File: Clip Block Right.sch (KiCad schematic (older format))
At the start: 18 parts, among them J16 Conn_01x08_Female, SW17 SW_SPST_4_PIN, SW18 SW_SPST_4_PIN, SW19 SW_SPST_4_PIN, SW20 SW_SPST_4_PIN, SW21 SW_SPST_4_PIN, SW22 SW_SPST_4_PIN, SW23 SW_SPST_4_PIN, SW24 SW_SPST_4_PIN, SW25 SW_SPST_4_PIN, SW26 SW_SPST_4_PIN, SW27 SW_SPST_4_PIN, SW28 SW_SPST_4_PIN, SW29 SW_SPST_4_PIN, SW30 SW_SPST_4_PIN, SW31 SW_SPST_4_PIN, SW32 SW_SPST_4_PIN, U2 CD74HC4067M

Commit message: Further work on the separate boards
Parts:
- SW17, SW18, SW19, SW20, SW21, SW22, SW23, SW24, SW25, SW26, SW27, SW28, SW29, SW30, SW31, SW32: symbol sw_spst_0:SW_SPST_4_PIN -> cp_midi_control_surface_002-rescue:SW_SPST_4_PIN-sw_spst_0
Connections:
- wire segments 114 -> 116
- no-connect marks 33 -> 32
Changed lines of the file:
@@
 $EndDescr
 $Comp
-L sw_spst_0:SW_SPST_4_PIN SW?
-U 1 1 5C60BB5B
-P 5550 1550
-AR Path="/5C4B73B3/5C60BB5B" Ref="SW?"  Part="1"
-AR Path="/5C4B9DB9/5C60BB5B" Ref="SW17"  Part="1"
-F 0 "SW17" H 5550 1300 50  0000 C CNN
-F 1 "SW_SPST_4_PIN" H 5550 1724 50  0001 C CNN
-F 2 "cunabulapress-footprints:Omron_B3F-5050" H 5550 1700 50  0001 C CNN
-F 3 "" H 5550 1700 50  0001 C CNN
-	1    5550 1550
-	1    0    0    -1
-$EndComp
-$Comp
-L sw_spst_0:SW_SPST_4_PIN SW?
+L cp_midi_control_surface_002-rescue:SW_SPST_4_PIN-sw_spst_0 SW?
 U 1 1 5C60BB62
 P 5550 2050
 AR Path="/5C4B73B3/5C60BB62" Ref="SW?"  Part="1"
 AR Path="/5C4B9DB9/5C60BB62" Ref="SW18"  Part="1"
+AR Path="/5C60BB62" Ref="SW18"  Part="1"
 F 0 "SW18" H 5550 1850 50  0000 C CNN
 F 1 "SW_SPST_4_PIN" H 5550 2224 50  0001 C CNN
@@
 $EndComp
 $Comp
-L sw_spst_0:SW_SPST_4_PIN SW?
+L cp_midi_control_surface_002-rescue:SW_SPST_4_PIN-sw_spst_0 SW?
 U 1 1 5C60BB69
 P 5550 2550
 AR Path="/5C4B73B3/5C60BB69" Ref="SW?"  Part="1"
 AR Path="/5C4B9DB9/5C60BB69" Ref="SW19"  Part="1"
+AR Path="/5C60BB69" Ref="SW19"  Part="1"
 F 0 "SW19" H 5550 2350 50  0000 C CNN
 F 1 "SW_SPST_4_PIN" H 5550 2724 50  0001 C CNN
@@
 $EndComp
 $Comp
-L sw_spst_0:SW_SPST_4_PIN SW?
+L cp_midi_control_surface_002-rescue:SW_SPST_4_PIN-sw_spst_0 SW?
 U 1 1 5C60BB70
 P 5550 3050
 AR Path="/5C4B73B3/5C60BB70" Ref="SW?"  Part="1"
 AR Path="/5C4B9DB9/5C60BB70" Ref="SW20"  Part="1"
+AR Path="/5C60BB70" Ref="SW20"  Part="1"
 F 0 "SW20" H 5550 2850 50  0000 C CNN
 F 1 "SW_SPST_4_PIN" H 5550 3224 50  0001 C CNN
@@
 $EndComp
 $Comp
-L sw_spst_0:SW_SPST_4_PIN SW?
+L cp_midi_control_surface_002-rescue:SW_SPST_4_PIN-sw_spst_0 SW?
 U 1 1 5C60BB77
 P 5550 3550
 AR Path="/5C4B73B3/5C60BB77" Ref="SW?"  Part="1"
 AR Path="/5C4B9DB9/5C60BB77" Ref="SW21"  Part="1"
+AR Path="/5C60BB77" Ref="SW21"  Part="1"
 F 0 "SW21" H 5550 3350 50  0000 C CNN
 F 1 "SW_SPST_4_PIN" H 5550 3724 50  0001 C CNN
@@
 $EndComp
 $Comp
-L sw_spst_0:SW_SPST_4_PIN SW?
+L cp_midi_control_surface_002-rescue:SW_SPST_4_PIN-sw_spst_0 SW?
 U 1 1 5C60BB7E
 P 5550 4050
 AR Path="/5C4B73B3/5C60BB7E" Ref="SW?"  Part="1"
 AR Path="/5C4B9DB9/5C60BB7E" Ref="SW22"  Part="1"
+AR Path="/5C60BB7E" Ref="SW22"  Part="1"
 F 0 "SW22" H 5550 3850 50  0000 C CNN
 F 1 "SW_SPST_4_PIN" H 5550 4224 50  0001 C CNN
@@
 $EndComp
 $Comp
-L sw_spst_0:SW_SPST_4_PIN SW?
+L cp_midi_control_surface_002-rescue:SW_SPST_4_PIN-sw_spst_0 SW?
 U 1 1 5C60BB85
 P 5550 4550
 AR Path="/5C4B73B3/5C60BB85" Ref="SW?"  Part="1"
 AR Path="/5C4B9DB9/5C60BB85" Ref="SW23"  Part="1"
+AR Path="/5C60BB85" Ref="SW23"  Part="1"
 F 0 "SW23" H 5550 4350 50  0000 C CNN
 F 1 "SW_SPST_4_PIN" H 5550 4724 50  0001 C CNN
@@
 $EndComp
 $Comp
-L sw_spst_0:SW_SPST_4_PIN SW?
+L cp_midi_control_surface_002-rescue:SW_SPST_4_PIN-sw_spst_0 SW?
 U 1 1 5C60BB8C
 P 5550 5050
 AR Path="/5C4B73B3/5C60BB8C" Ref="SW?"  Part="1"
 AR Path="/5C4B9DB9/5C60BB8C" Ref="SW24"  Part="1"
+AR Path="/5C60BB8C" Ref="SW24"  Part="1"
 F 0 "SW24" H 5550 4850 50  0000 C CNN
 F 1 "SW_SPST_4_PIN" H 5550 5224 50  0001 C CNN
@@
 $EndComp
 $Comp
-L sw_spst_0:SW_SPST_4_PIN SW?
+L cp_midi_control_surface_002-rescue:SW_SPST_4_PIN-sw_spst_0 SW?
 U 1 1 5C60BB93
 P 4050 2350
 AR Path="/5C4B73B3/5C60BB93" Ref="SW?"  Part="1"
 AR Path="/5C4B9DB9/5C60BB93" Ref="SW25"  Part="1"
+AR Path="/5C60BB93" Ref="SW25"  Part="1"
 F 0 "SW25" H 4050 2150 50  0000 C CNN
 F 1 "SW_SPST_4_PIN" H 4750 2300 50  0001 C CNN
@@
 $EndComp
 $Comp
-L sw_spst_0:SW_SPST_4_PIN SW?
+L cp_midi_control_surface_002-rescue:SW_SPST_4_PIN-sw_spst_0 SW?
 U 1 1 5C60BB9A
 P 4050 2850
 AR Path="/5C4B73B3/5C60BB9A" Ref="SW?"  Part="1"
 AR Path="/5C4B9DB9/5C60BB9A" Ref="SW26"  Part="1"
+AR Path="/5C60BB9A" Ref="SW26"  Part="1"
 F 0 "SW26" H 4050 2650 50  0000 C CNN
 F 1 "SW_SPST_4_PIN" H 4050 3024 50  0001 C CNN
@@
 $EndComp
 $Comp
-L sw_spst_0:SW_SPST_4_PIN SW?
+L cp_midi_control_surface_002-rescue:SW_SPST_4_PIN-sw_spst_0 SW?
 U 1 1 5C60BBA8
 P 4050 3850
 AR Path="/5C4B73B3/5C60BBA8" Ref="SW?"  Part="1"
 AR Path="/5C4B9DB9/5C60BBA8" Ref="SW28"  Part="1"
+AR Path="/5C60BBA8" Ref="SW28"  Part="1"
 F 0 "SW28" H 4050 3650 50  0000 C CNN
 F 1 "SW_SPST_4_PIN" H 4050 4024 50  0001 C CNN
@@
 $EndComp
 $Comp
-L sw_spst_0:SW_SPST_4_PIN SW?
+L cp_midi_control_surface_002-rescue:SW_SPST_4_PIN-sw_spst_0 SW?
 U 1 1 5C60BBAF
 P 4050 4350
 AR Path="/5C4B73B3/5C60BBAF" Ref="SW?"  Part="1"
 AR Path="/5C4B9DB9/5C60BBAF" Ref="SW29"  Part="1"
+AR Path="/5C60BBAF" Ref="SW29"  Part="1"
 F 0 "SW29" H 4050 4150 50  0000 C CNN
 F 1 "SW_SPST_4_PIN" H 4050 4524 50  0001 C CNN
@@
 $EndComp
 $Comp
-L sw_spst_0:SW_SPST_4_PIN SW?
+L cp_midi_control_surface_002-rescue:SW_SPST_4_PIN-sw_spst_0 SW?
 U 1 1 5C60BBB6
 P 4050 4850
 AR Path="/5C4B73B3/5C60BBB6" Ref="SW?"  Part="1"
 AR Path="/5C4B9DB9/5C60BBB6" Ref="SW30"  Part="1"
+AR Path="/5C60BBB6" Ref="SW30"  Part="1"
 F 0 "SW30" H 4050 4650 50  0000 C CNN
 F 1 "SW_SPST_4_PIN" H 4050 5024 50  0001 C CNN
@@
 $EndComp
 $Comp
-L sw_spst_0:SW_SPST_4_PIN SW?
+L cp_midi_control_surface_002-rescue:SW_SPST_4_PIN-sw_spst_0 SW?
 U 1 1 5C60BBBD
 P 4050 5350
 AR Path="/5C4B73B3/5C60BBBD" Ref="SW?"  Part="1"
 AR Path="/5C4B9DB9/5C60BBBD" Ref="SW31"  Part="1"
+AR Path="/5C60BBBD" Ref="SW31"  Part="1"
 F 0 "SW31" H 4050 5150 50  0000 C CNN
 F 1 "SW_SPST_4_PIN" H 4050 5524 50  0001 C CNN
@@
 $EndComp
 $Comp
-L sw_spst_0:SW_SPST_4_PIN SW?
+L cp_midi_control_surface_002-rescue:SW_SPST_4_PIN-sw_spst_0 SW?
 U 1 1 5C60BBC4
 P 4050 5850
 AR Path="/5C4B73B3/5C60BBC4" Ref="SW?"  Part="1"
 AR Path="/5C4B9DB9/5C60BBC4" Ref="SW32"  Part="1"
+AR Path="/5C60BBC4" Ref="SW32"  Part="1"
 F 0 "SW32" H 4050 5650 50  0000 C CNN
 F 1 "SW_SPST_4_PIN" H 4050 6024 50  0001 C CNN
@@
 	2650 2750 3400 2750
 Wire Wire Line
-	3400 2750 3400 4350
-Wire Wire Line
-	3400 4350 3850 4350
-Wire Wire Line
 	2650 2850 3300 2850
-Wire Wire Line
-	3300 2850 3300 4850
-Wire Wire Line
-	3300 4850 3850 4850
 Wire Wire Line
 	2650 2950 3200 2950
@@
 	3500 1800 4800 1800
 Wire Wire Line
-	5000 1700 5000 3050
-Wire Wire Line
-	5100 1650 5100 2550
-Wire Wire Line
-	5200 1600 5200 2050
-Wire Wire Line
-	5200 2050 5350 2050
-Wire Wire Line
-	2650 1550 5350 1550
-Wire Wire Line
-	5100 2550 5350 2550
-Wire Wire Line
-	5000 3050 5350 3050
+	2650 1550 5300 1550
 Wire Wire Line
 	3100 1600 5200 1600
@@
 Wire Wire Line
 	2150 3450 2150 3350
-NoConn ~ 5350 1650
-NoConn ~ 5350 2150
-NoConn ~ 5350 2650
-NoConn ~ 5350 3150
 NoConn ~ 5750 4150
 NoConn ~ 5750 3650
@@
 NoConn ~ 4250 3950
 NoConn ~ 4250 4450
-NoConn ~ 3850 4450
-NoConn ~ 3850 4950
 NoConn ~ 4250 4950
 NoConn ~ 4250 5450
@@
 	2650 2350 3800 2350
 $Comp
-L sw_spst_0:SW_SPST_4_PIN SW?
+L cp_midi_control_surface_002-rescue:SW_SPST_4_PIN-sw_spst_0 SW?
 U 1 1 5C60BBA1
 P 4050 3350
 AR Path="/5C4B73B3/5C60BBA1" Ref="SW?"  Part="1"
 AR Path="/5C4B9DB9/5C60BBA1" Ref="SW27"  Part="1"
+AR Path="/5C60BBA1" Ref="SW27"  Part="1"
 F 0 "SW27" H 4050 3150 50  0000 C CNN
 F 1 "SW_SPST_4_PIN" H 4050 3524 50  0001 C CNN
@@
 	3500 2650 3500 3950
 Wire Wire Line
-	4900 3650 5350 3650
-Wire Wire Line
-	4900 1750 4900 3650
-Wire Wire Line
-	4800 4150 5350 4150
-Wire Wire Line
-	4800 1800 4800 4150
+	4900 1750 4900 3550
+Wire Wire Line
+	4800 1800 4800 4050
 Wire Wire Line
 	4700 1850 4700 4550
-Wire Wire Line
-	4600 5150 5350 5150
-Wire Wire Line
-	4600 1900 4600 5150
-NoConn ~ 5350 3550
-NoConn ~ 5350 4050
-NoConn ~ 5350 5050
 Wire Wire Line
 	4700 4550 5350 4550
@@
 	5900 5150 5900 5850
 NoConn ~ 5750 5050
+Wire Wire Line
+	5350 2150 5200 2150
+Wire Wire Line
+	5200 1600 5200 2150
+Wire Wire Line
+	3400 2750 3400 4350
+Wire Wire Line
+	5350 5050 4600 5050
+Wire Wire Line
+	4600 1900 4600 5050
+Wire Wire Line
+	5300 1550 5300 1650
+Wire Wire Line
+	5300 1650 5350 1650
+$Comp
+L cp_midi_control_surface_002-rescue:SW_SPST_4_PIN-sw_spst_0 SW?
+U 1 1 5C60BB5B
+P 5550 1550
+AR Path="/5C4B73B3/5C60BB5B" Ref="SW?"  Part="1"
+AR Path="/5C4B9DB9/5C60BB5B" Ref="SW17"  Part="1"
+AR Path="/5C60BB5B" Ref="SW17"  Part="1"
+F 0 "SW17" H 5550 1300 50  0000 C CNN
+F 1 "SW_SPST_4_PIN" H 5550 1724 50  0001 C CNN
+F 2 "cunabulapress-footprints:Omron_B3F-5050" H 5550 1700 50  0001 C CNN
+F 3 "" H 5550 1700 50  0001 C CNN
+	1    5550 1550
+	1    0    0    -1
+$EndComp
+NoConn ~ 5350 2050
+NoConn ~ 5350 1550
+Wire Wire Line
+	5350 2650 5100 2650
+Wire Wire Line
+	5100 1650 5100 2650
+Wire Wire Line
+	5350 3150 5000 3150
+Wire Wire Line
+	5000 1700 5000 3150
+Wire Wire Line
+	5350 3550 4900 3550
+NoConn ~ 5350 3650
+NoConn ~ 5350 3050
+NoConn ~ 5350 2550
+NoConn ~ 5350 4150
+Wire Wire Line
+	5350 4050 4800 4050
+Wire Wire Line
+	3850 4350 3400 4350
+Wire Wire Line
+	3850 4850 3300 4850
+Wire Wire Line
+	3300 2850 3300 4850
+NoConn ~ 3850 4450
+NoConn ~ 3850 4950
 $EndSCHEMATC

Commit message: Sub boards completed
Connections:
- net at U2.13 (S3): now also J16.3 (Pin_3); no longer J16.4 (Pin_4)
- net at U2.14 (S2): now also J16.4 (Pin_4); no longer J16.3 (Pin_3)
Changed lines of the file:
@@
 NoConn ~ 700  2850
-Wire Wire Line
-	700  2450 1650 2450
 Wire Wire Line
 	700  2150 1650 2150
 Wire Wire Line
 	700  2250 1650 2250
-Wire Wire Line
-	700  2350 1650 2350
 Wire Wire Line
 	1350 2550 1350 1750
@@
 NoConn ~ 3850 4450
 NoConn ~ 3850 4950
+Wire Wire Line
+	1050 2450 1050 2350
+Wire Wire Line
+	1050 2350 700  2350
+Wire Wire Line
+	1050 2450 1650 2450
+Wire Wire Line
+	700  2450 850  2450
+Wire Wire Line
+	850  2450 850  2400
+Wire Wire Line
+	850  2400 1200 2400
+Wire Wire Line
+	1200 2400 1200 2350
+Wire Wire Line
+	1200 2350 1650 2350
 $EndSCHEMATC

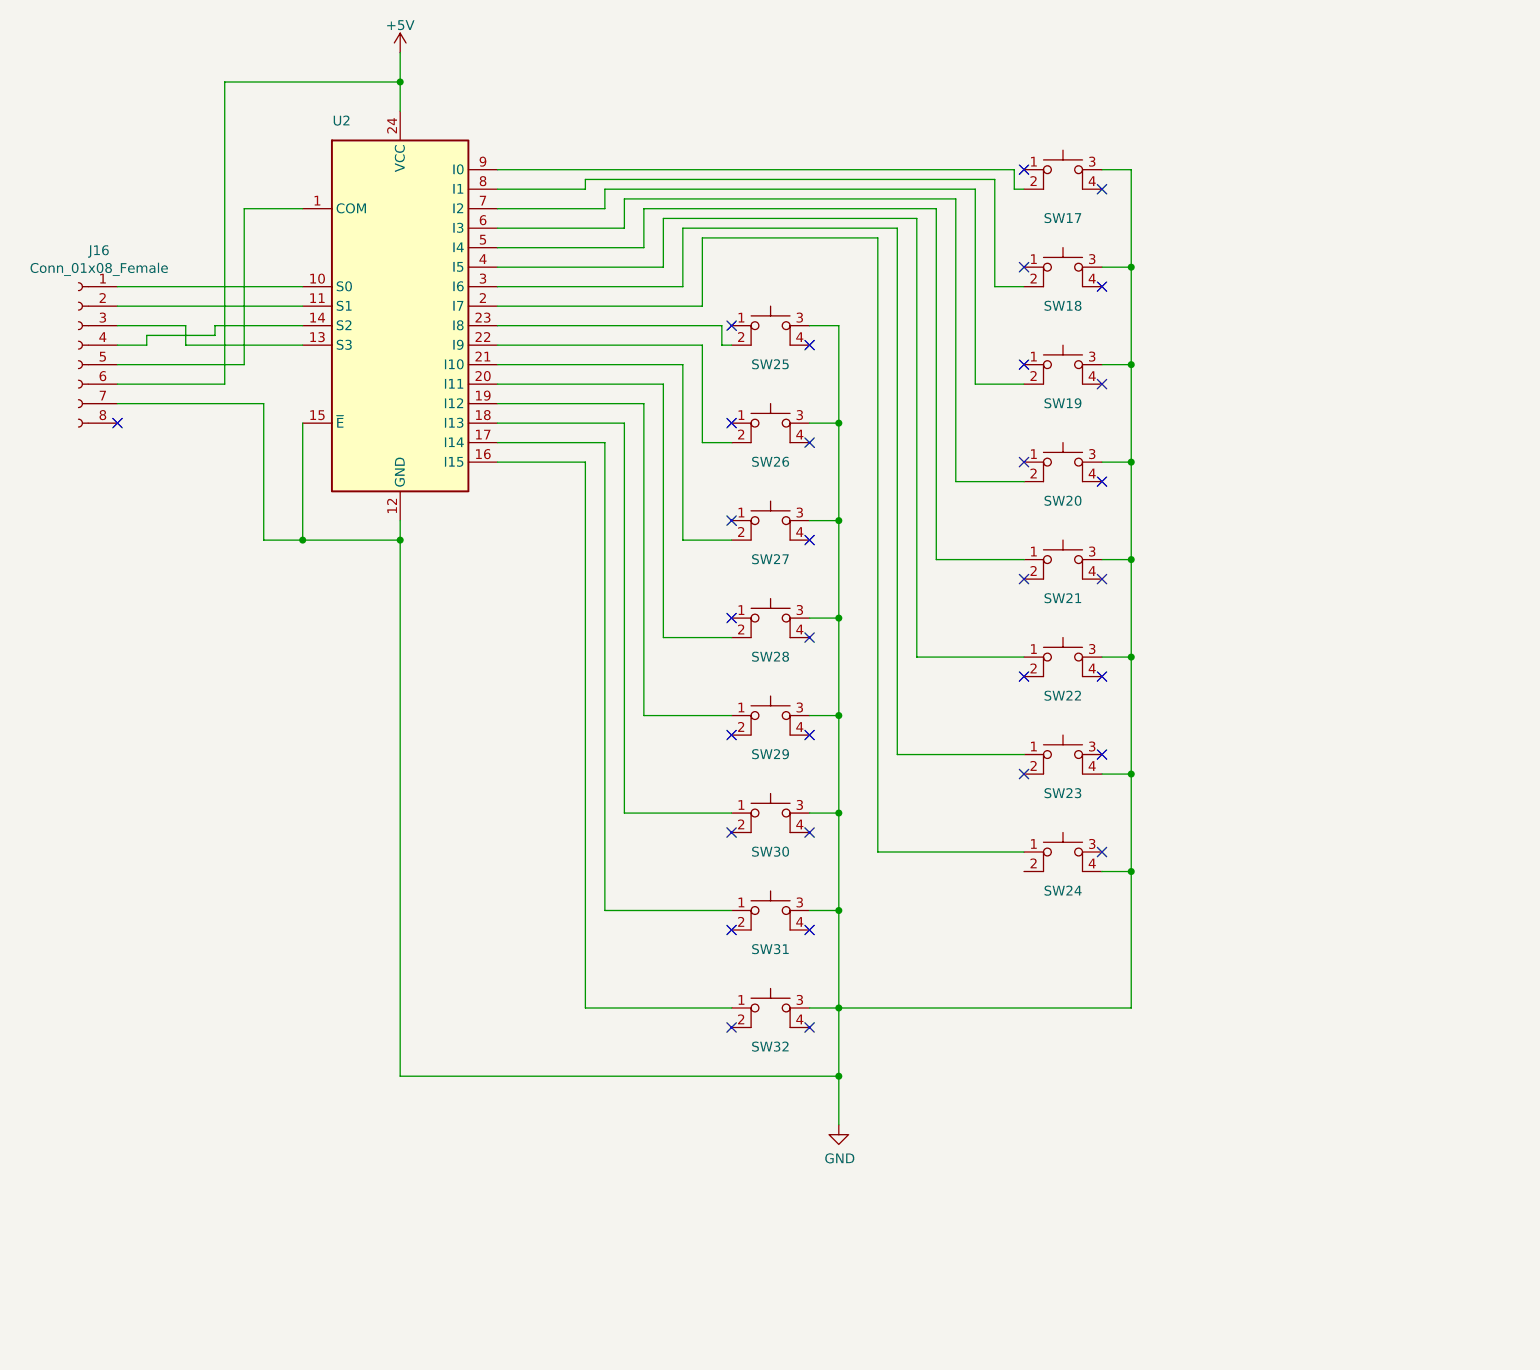
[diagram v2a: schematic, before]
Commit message: Tidy schematic / renumber components / complete daughter boards
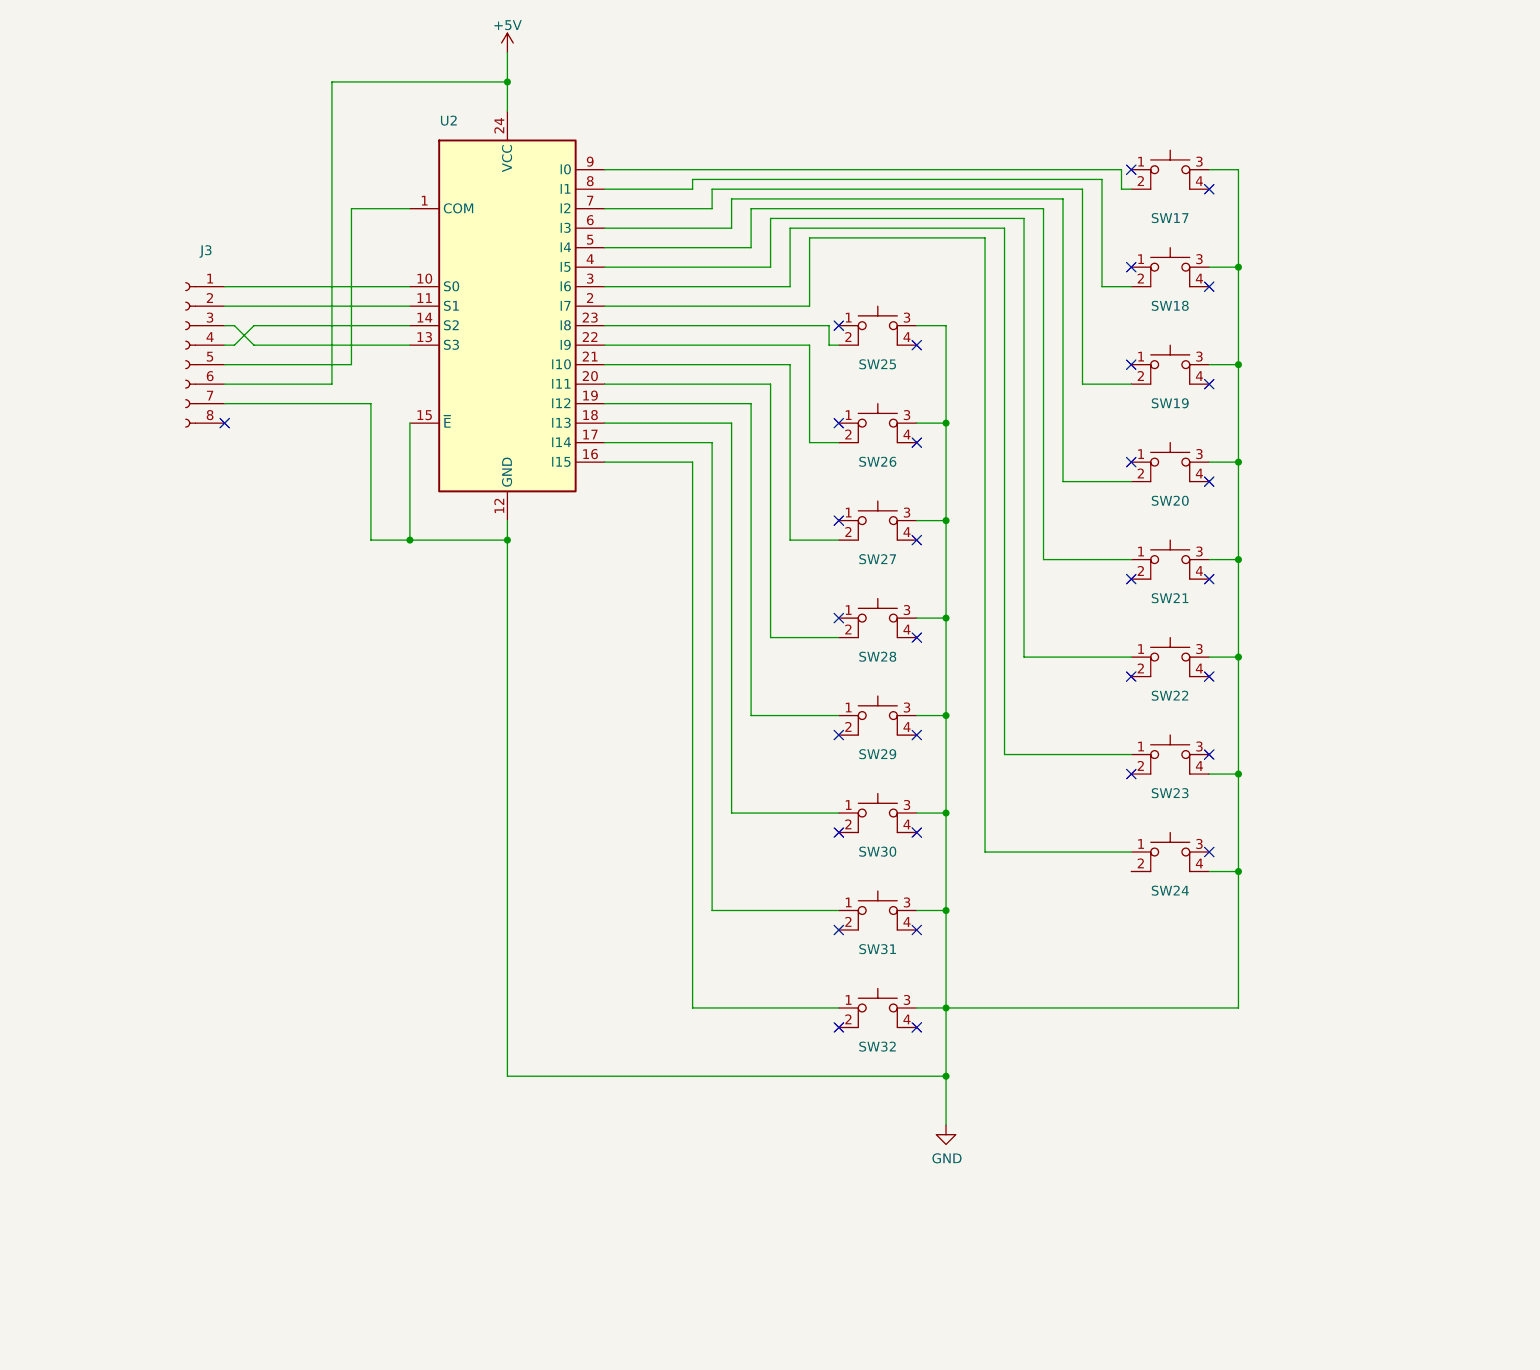
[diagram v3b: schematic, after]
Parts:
- J3: renamed from J16; value Conn_01x08_Female -> ~
- SW17, SW18, SW19, SW20, SW21, SW22, SW23, SW24, SW25, SW26, SW27, SW28, SW29, SW30, SW31, SW32: value SW_SPST_4_PIN -> B3F-5050
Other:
- moved on the sheet: J3, SW17, SW18, SW19, SW20, SW21, SW22, SW23, SW24, SW25, SW26, SW27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
